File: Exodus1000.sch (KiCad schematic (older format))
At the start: 5 parts, among them J1 ARJ-169, M1 ET60S-02-24-02-X-VP-GP, M2 ET60S-02-24-02-X-VP-GP, M3 ET60S-02-24-02-X-VP-GP, M4 ET60S-02-24-02-X-VP-GP

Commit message: added some more stuff
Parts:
- removed J1: ARJ-169, Exodus_Connectors:ARJ-169, symbol Exodus_Connectors:ARJ-169
- removed M1, M2, M3, M4: ET60S-02-24-02-X-VP-GP, Exodus_Connectors:ET60S-02-24-02-X-VP-GP, symbol ET60S-02-24-02-X-VP-GP:ET60S-02-24-02-X-VP-GP
- added U4: TUSB4041I, Package_QFP:HTQFP-64-1EP_10x10mm_P0.5mm_EP8x8mm_Mask4.4x4.4mm_ThermalVias, symbol Interface_USB:TUSB4041I
- added U5: FSUSB42UMX, Package_DFN_QFN:MLPQ-16-1EP_4x4mm_P0.65mm_EP2.8x2.8mm, symbol FSUSB42UMX:FSUSB42UMX
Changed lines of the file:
@@
 $Descr A4 11693 8268
 encoding utf-8
-Sheet 1 3
+Sheet 1 4
 Title ""
 Date ""
@@
 Comment4 ""
 $EndDescr
-$Comp
-L ET60S-02-24-02-X-VP-GP:ET60S-02-24-02-X-VP-GP M2
-U 1 1 5C80BFD4
-P 9750 1100
-F 0 "M2" H 10278 -8  45  0000 L CNN
-F 1 "ET60S-02-24-02-X-VP-GP" H 10278 -92 45  0000 L CNN
-F 2 "Exodus_Connectors:ET60S-02-24-02-X-VP-GP" H 9780 1250 20  0001 C CNN
-F 3 "" H 9750 1100 50  0001 C CNN
-	1    9750 1100
-	1    0    0    -1
-$EndComp
-$Comp
-L ET60S-02-24-02-X-VP-GP:ET60S-02-24-02-X-VP-GP M2
-U 2 1 5C80C056
-P 8300 1350
-F 0 "M2" H 8750 1604 45  0000 C CNN
-F 1 "ET60S-02-24-02-X-VP-GP" H 8750 1520 45  0000 C CNN
-F 2 "Exodus_Connectors:ET60S-02-24-02-X-VP-GP" H 8330 1500 20  0001 C CNN
-F 3 "" H 8300 1350 50  0001 C CNN
-	2    8300 1350
-	1    0    0    -1
-$EndComp
-$Comp
-L ET60S-02-24-02-X-VP-GP:ET60S-02-24-02-X-VP-GP M1
-U 1 1 5C80C304
-P 1100 950
-F 0 "M1" H 1628 -158 45  0000 L CNN
-F 1 "ET60S-02-24-02-X-VP-GP" H 1628 -242 45  0000 L CNN
-F 2 "Exodus_Connectors:ET60S-02-24-02-X-VP-GP" H 1130 1100 20  0001 C CNN
-F 3 "" H 1100 950 50  0001 C CNN
-	1    1100 950
-	1    0    0    -1
-$EndComp
-$Comp
-L ET60S-02-24-02-X-VP-GP:ET60S-02-24-02-X-VP-GP M1
-U 2 1 5C80C3A6
-P 2050 1200
-F 0 "M1" H 2500 1454 45  0000 C CNN
-F 1 "ET60S-02-24-02-X-VP-GP" H 2500 1370 45  0000 C CNN
-F 2 "Exodus_Connectors:ET60S-02-24-02-X-VP-GP" H 2080 1350 20  0001 C CNN
-F 3 "" H 2050 1200 50  0001 C CNN
-	2    2050 1200
-	1    0    0    -1
-$EndComp
-$Comp
-L ET60S-02-24-02-X-VP-GP:ET60S-02-24-02-X-VP-GP M3
-U 1 1 5C80C5DA
-P 1100 3850
-F 0 "M3" H 1628 2742 45  0000 L CNN
-F 1 "ET60S-02-24-02-X-VP-GP" H 1628 2658 45  0000 L CNN
-F 2 "Exodus_Connectors:ET60S-02-24-02-X-VP-GP" H 1130 4000 20  0001 C CNN
-F 3 "" H 1100 3850 50  0001 C CNN
-	1    1100 3850
-	1    0    0    -1
-$EndComp
-$Comp
-L ET60S-02-24-02-X-VP-GP:ET60S-02-24-02-X-VP-GP M3
-U 2 1 5C80C63C
-P 2050 4050
-F 0 "M3" H 2500 4304 45  0000 C CNN
-F 1 "ET60S-02-24-02-X-VP-GP" H 2500 4220 45  0000 C CNN
-F 2 "Exodus_Connectors:ET60S-02-24-02-X-VP-GP" H 2080 4200 20  0001 C CNN
-F 3 "" H 2050 4050 50  0001 C CNN
-	2    2050 4050
-	1    0    0    -1
-$EndComp
-$Comp
-L ET60S-02-24-02-X-VP-GP:ET60S-02-24-02-X-VP-GP M4
-U 2 1 5C80C6A4
-P 8300 4150
-F 0 "M4" H 8750 4404 45  0000 C CNN
-F 1 "ET60S-02-24-02-X-VP-GP" H 8750 4320 45  0000 C CNN
-F 2 "Exodus_Connectors:ET60S-02-24-02-X-VP-GP" H 8330 4300 20  0001 C CNN
-F 3 "" H 8300 4150 50  0001 C CNN
-	2    8300 4150
-	1    0    0    -1
-$EndComp
-$Comp
-L ET60S-02-24-02-X-VP-GP:ET60S-02-24-02-X-VP-GP M4
-U 1 1 5C80C70C
-P 9800 3800
-F 0 "M4" H 10328 2692 45  0000 L CNN
-F 1 "ET60S-02-24-02-X-VP-GP" H 10328 2608 45  0000 L CNN
-F 2 "Exodus_Connectors:ET60S-02-24-02-X-VP-GP" H 9830 3950 20  0001 C CNN
-F 3 "" H 9800 3800 50  0001 C CNN
-	1    9800 3800
-	1    0    0    -1
-$EndComp
-$Comp
-L Exodus_Connectors:ARJ-169 J1
-U 1 1 5C80A95E
-P 7050 1750
-F 0 "J1" H 7050 2575 50  0000 C CNN
-F 1 "ARJ-169" H 7050 2484 50  0000 C CNN
-F 2 "Exodus_Connectors:ARJ-169" H 7200 1950 50  0001 C CNN
-F 3 "" H 7200 1950 50  0001 C CNN
-	1    7050 1750
-	1    0    0    -1
-$EndComp
-$Comp
-L Exodus_Connectors:ARJ-169 J1
-U 2 1 5C80A9FB
-P 7050 3150
-F 0 "J1" H 7050 3748 50  0000 C CNN
-F 1 "ARJ-169" H 7050 3657 50  0000 C CNN
-F 2 "Exodus_Connectors:ARJ-169" H 7200 3350 50  0001 C CNN
-F 3 "" H 7200 3350 50  0001 C CNN
-	2    7050 3150
-	1    0    0    -1
-$EndComp
 $Sheet
-S 3900 3250 850  850
+S 3300 2250 850  850
 U 5C80AE96
 F0 "TM4C129" 50
@@
 $EndSheet
 $Sheet
-S 5450 4250 900  800
+S 2750 3800 900  800
 U 5C80E9D1
 F0 "ft232h" 50
 F1 "ft232h.sch" 50
 $EndSheet
+$Sheet
+S 1250 2150 950  850
+U 5C8128A2
+F0 "Connectors" 50
+F1 "connectors.sch" 50
+$EndSheet
+$Comp
+L Interface_USB:TUSB4041I U4
+U 1 1 5C81313F
+P 6450 3450
+F 0 "U4" H 6450 1264 50  0000 C CNN
+F 1 "TUSB4041I" H 6450 1173 50  0000 C CNN
+F 2 "Package_QFP:HTQFP-64-1EP_10x10mm_P0.5mm_EP8x8mm_Mask4.4x4.4mm_ThermalVias" H 7650 5450 50  0001 L CNN
+F 3 "http://www.ti.com/lit/ds/symlink/tusb4041i.pdf" H 6150 3650 50  0001 C CNN
+	1    6450 3450
+	1    0    0    -1
+$EndComp
+$Comp
+L FSUSB42UMX:FSUSB42UMX U5
+U 1 1 5C81F656
+P 3050 6000
+F 0 "U5" H 3050 6767 50  0000 C CNN
+F 1 "FSUSB42UMX" H 3050 6676 50  0000 C CNN
+F 2 "Package_DFN_QFN:MLPQ-16-1EP_4x4mm_P0.65mm_EP2.8x2.8mm" H 3050 6000 50  0001 L BNN
+F 3 "ON Semiconductor" H 3050 6000 50  0001 L BNN
+F 4 "None" H 3050 6000 50  0001 L BNN "Field4"
+F 5 "Unavailable" H 3050 6000 50  0001 L BNN "Field5"
+F 6 "FSUSB42UMX" H 3050 6000 50  0001 L BNN "Field6"
+F 7 "UFQFN-10 ON Semiconductor" H 3050 6000 50  0001 L BNN "Field7"
+F 8 "FSUSB42 Series DPDT 4.3 V 480 Mbps SMT Hi Speed USB 2.0 Switch - UMLP-10" H 3050 6000 50  0001 L BNN "Field8"
+	1    3050 6000
+	1    0    0    -1
+$EndComp
 $EndSCHEMATC

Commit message: layout stuff
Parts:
- removed U4: TUSB4041I, Package_QFP:HTQFP-64-1EP_10x10mm_P0.5mm_EP8x8mm_Mask4.4x4.4mm_ThermalVias, symbol Interface_USB:TUSB4041I
- removed U5: FSUSB42UMX, Package_DFN_QFN:MLPQ-16-1EP_4x4mm_P0.65mm_EP2.8x2.8mm, symbol FSUSB42UMX:FSUSB42UMX
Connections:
- wire segments 0 -> 24
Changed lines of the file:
@@
 $EndDescr
 $Sheet
-S 3300 2250 850  850
+S 5450 2050 900  1450
 U 5C80AE96
 F0 "TM4C129" 50
 F1 "tm4c129.sch" 50
+F2 "ETH_RXI_N" I L 5450 2150 50
+F3 "ETH_RXI_P" I L 5450 2250 50
+F4 "ETH_TXO_N" I L 5450 2350 50
+F5 "ETH_TXO_P" I L 5450 2450 50
+F6 "JTAG_TCK" I R 6350 3100 50
+F7 "JTAG_TMS" I R 6350 3200 50
+F8 "JTAG_TDI" I R 6350 3300 50
+F9 "JTAG_TDO" I R 6350 3400 50
+F10 "USB_D_N" I L 5450 3050 50
+F11 "USB_D_P" I L 5450 3150 50
+F12 "USB_ID" I L 5450 3250 50
 $EndSheet
 $Sheet
-S 2750 3800 900  800
+S 5500 4250 900  800
 U 5C80E9D1
 F0 "ft232h" 50
 F1 "ft232h.sch" 50
+F2 "D-" I L 5500 4400 50
+F3 "D+" I L 5500 4500 50
 $EndSheet
 $Sheet
-S 1250 2150 950  850
+S 3850 2850 950  1350
 U 5C8128A2
 F0 "Connectors" 50
 F1 "connectors.sch" 50
+F2 "USB_OTG_N" I R 4800 3450 50
+F3 "USB_OTG_P" I R 4800 3550 50
+F4 "USB_JTAG_P" I R 4800 4000 50
+F5 "USB_JTAG_N" I R 4800 3900 50
+F6 "TD_P" I R 4800 3250 50
+F7 "TD_N" I R 4800 3150 50
+F8 "RD_P" I R 4800 3000 50
+F9 "RD_N" I R 4800 2900 50
 $EndSheet
-$Comp
-L Interface_USB:TUSB4041I U4
-U 1 1 5C81313F
-P 6450 3450
-F 0 "U4" H 6450 1264 50  0000 C CNN
-F 1 "TUSB4041I" H 6450 1173 50  0000 C CNN
-F 2 "Package_QFP:HTQFP-64-1EP_10x10mm_P0.5mm_EP8x8mm_Mask4.4x4.4mm_ThermalVias" H 7650 5450 50  0001 L CNN
-F 3 "http://www.ti.com/lit/ds/symlink/tusb4041i.pdf" H 6150 3650 50  0001 C CNN
-	1    6450 3450
-	1    0    0    -1
-$EndComp
-$Comp
-L FSUSB42UMX:FSUSB42UMX U5
-U 1 1 5C81F656
-P 3050 6000
-F 0 "U5" H 3050 6767 50  0000 C CNN
-F 1 "FSUSB42UMX" H 3050 6676 50  0000 C CNN
-F 2 "Package_DFN_QFN:MLPQ-16-1EP_4x4mm_P0.65mm_EP2.8x2.8mm" H 3050 6000 50  0001 L BNN
-F 3 "ON Semiconductor" H 3050 6000 50  0001 L BNN
-F 4 "None" H 3050 6000 50  0001 L BNN "Field4"
-F 5 "Unavailable" H 3050 6000 50  0001 L BNN "Field5"
-F 6 "FSUSB42UMX" H 3050 6000 50  0001 L BNN "Field6"
-F 7 "UFQFN-10 ON Semiconductor" H 3050 6000 50  0001 L BNN "Field7"
-F 8 "FSUSB42 Series DPDT 4.3 V 480 Mbps SMT Hi Speed USB 2.0 Switch - UMLP-10" H 3050 6000 50  0001 L BNN "Field8"
-	1    3050 6000
-	1    0    0    -1
-$EndComp
+Wire Wire Line
+	4800 4000 4950 4000
+Wire Wire Line
+	4950 4000 4950 4500
+Wire Wire Line
+	4950 4500 5500 4500
+Wire Wire Line
+	5500 4400 5100 4400
+Wire Wire Line
+	5100 4400 5100 3900
+Wire Wire Line
+	5100 3900 4800 3900
+Wire Wire Line
+	4800 3450 5150 3450
+Wire Wire Line
+	5150 3450 5150 3050
+Wire Wire Line
+	5150 3050 5450 3050
+Wire Wire Line
+	5450 3150 5250 3150
+Wire Wire Line
+	5250 3150 5250 3550
+Wire Wire Line
+	5250 3550 4800 3550
+Wire Wire Line
+	4800 2900 4850 2900
+Wire Wire Line
+	4850 2900 4850 2150
+Wire Wire Line
+	4850 2150 5450 2150
+Wire Wire Line
+	5450 2250 4900 2250
+Wire Wire Line
+	4900 2250 4900 3000
+Wire Wire Line
+	4900 3000 4800 3000
+Wire Wire Line
+	4800 3150 5000 3150
+Wire Wire Line
+	5000 3150 5000 2350
+Wire Wire Line
+	5000 2350 5450 2350
+Wire Wire Line
+	5450 2450 5050 2450
+Wire Wire Line
+	5050 2450 5050 3250
+Wire Wire Line
+	5050 3250 4800 3250
 $EndSCHEMATC

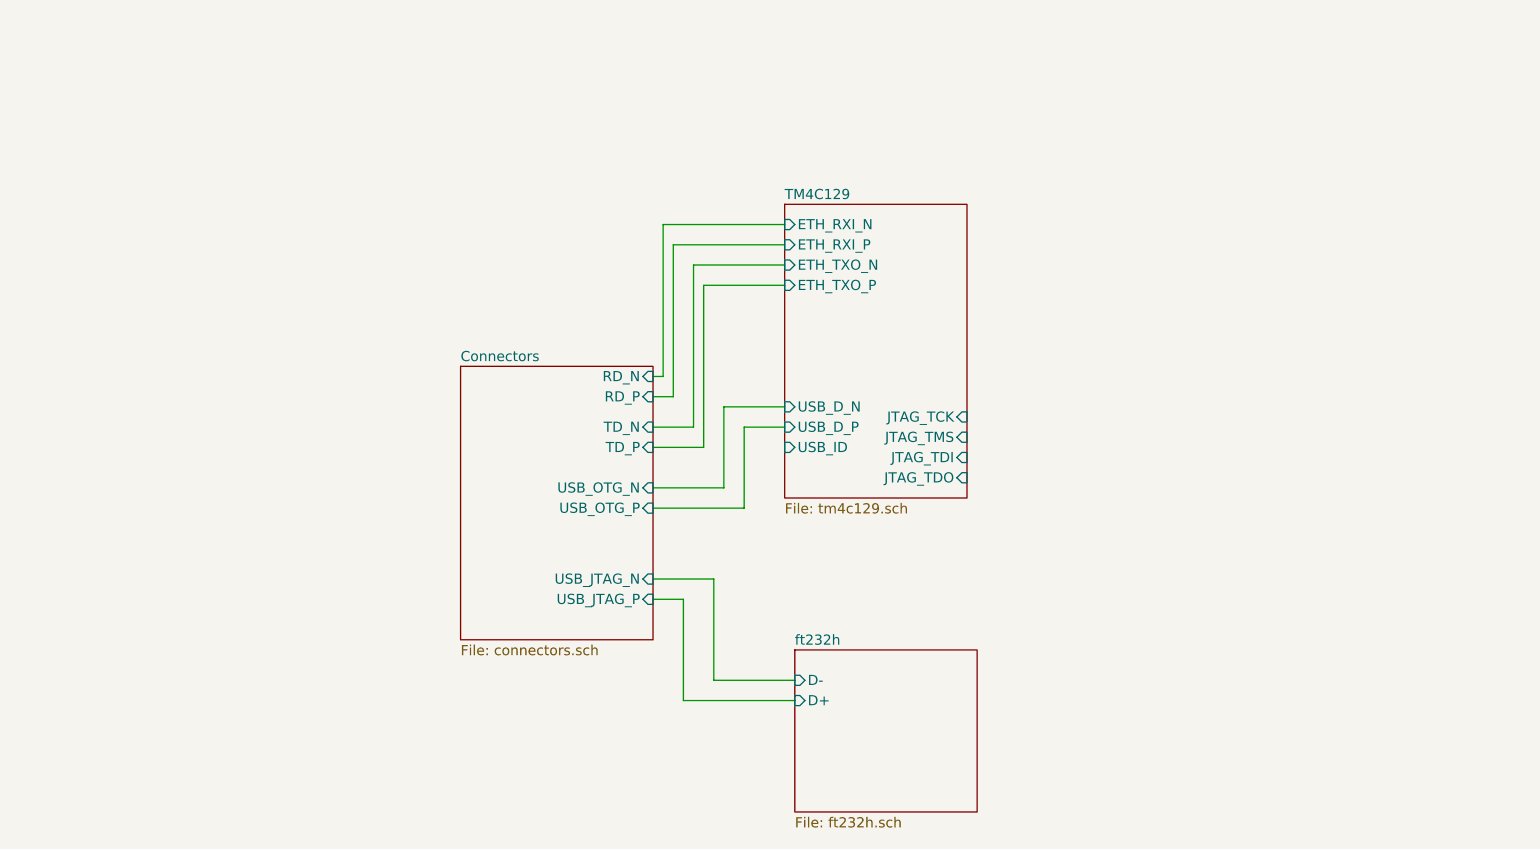
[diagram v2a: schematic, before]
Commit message: usb hub and sdram selected.
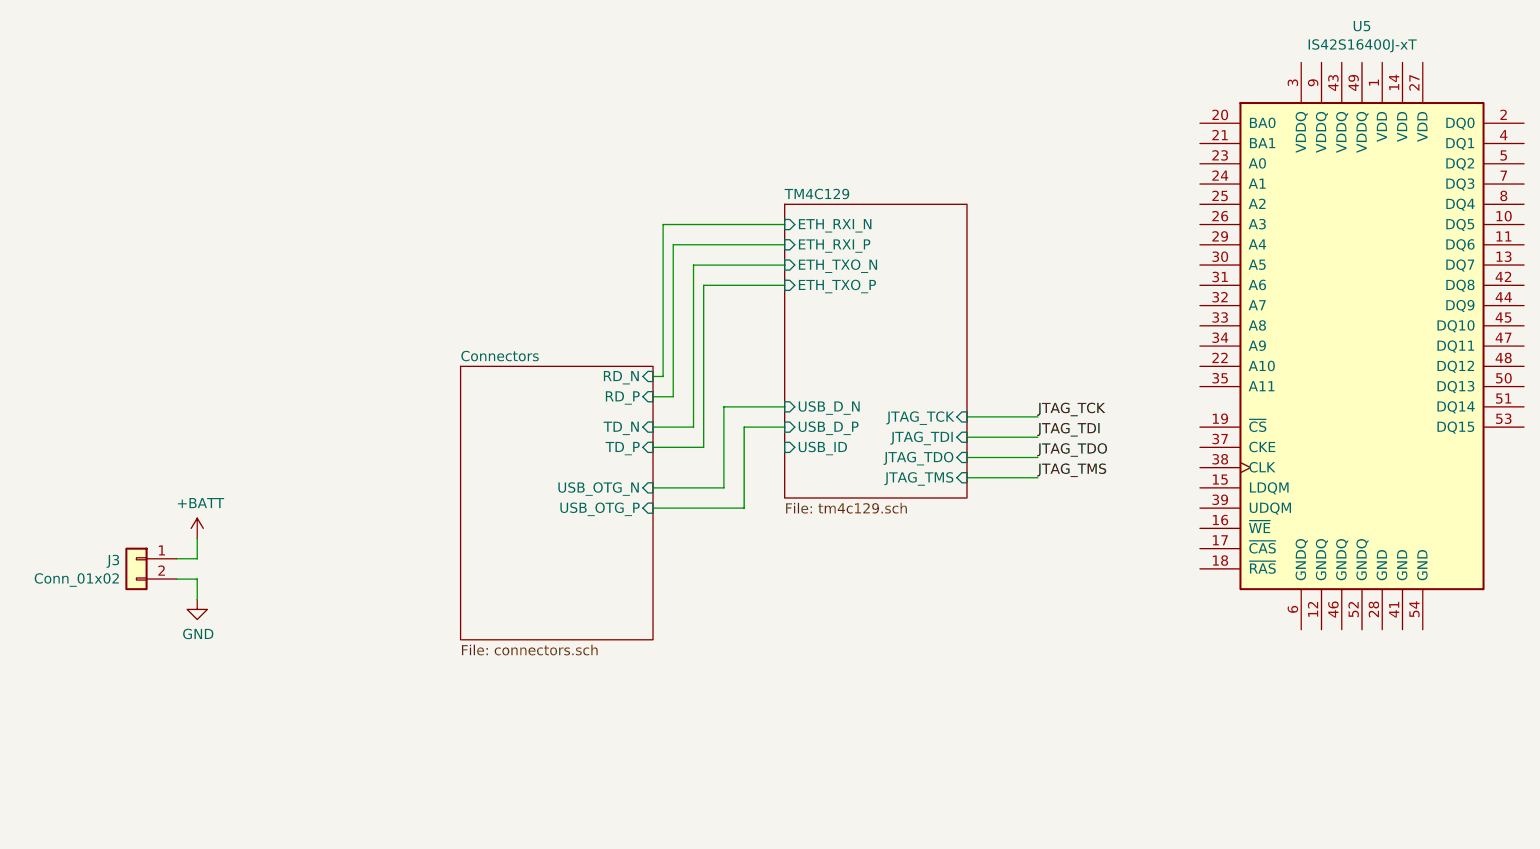
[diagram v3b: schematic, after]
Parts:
- added J3: Conn_01x02, Connector_PinHeader_2.54mm:PinHeader_1x02_P2.54mm_Horizontal, symbol Connector_Generic:Conn_01x02
- added U5: IS42S16400J-xT, Package_SO:TSOP-II-54_22.2x10.16mm_P0.8mm, symbol Memory_RAM:IS42S16400J-xT
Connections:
- new net +BATT: J3.1 (Pin_1)
- new net GND: J3.2 (Pin_2)
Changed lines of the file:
@@
 $Descr A4 11693 8268
 encoding utf-8
-Sheet 1 4
-Title ""
-Date ""
-Rev ""
-Comp ""
+Sheet 1 5
+Title "Exodus1000"
+Date "2019-03-16"
+Rev "A"
+Comp "Exodus"
 Comment1 ""
 Comment2 ""
@@
 F5 "ETH_TXO_P" I L 5450 2450 50
 F6 "JTAG_TCK" I R 6350 3100 50
-F7 "JTAG_TMS" I R 6350 3200 50
-F8 "JTAG_TDI" I R 6350 3300 50
-F9 "JTAG_TDO" I R 6350 3400 50
+F7 "JTAG_TMS" I R 6350 3400 50
+F8 "JTAG_TDI" I R 6350 3200 50
+F9 "JTAG_TDO" I R 6350 3300 50
 F10 "USB_D_N" I L 5450 3050 50
 F11 "USB_D_P" I L 5450 3150 50
 F12 "USB_ID" I L 5450 3250 50
-$EndSheet
-$Sheet
-S 5500 4250 900  800
-U 5C80E9D1
-F0 "ft232h" 50
-F1 "ft232h.sch" 50
-F2 "D-" I L 5500 4400 50
-F3 "D+" I L 5500 4500 50
 $EndSheet
 $Sheet
@@
 F2 "USB_OTG_N" I R 4800 3450 50
 F3 "USB_OTG_P" I R 4800 3550 50
-F4 "USB_JTAG_P" I R 4800 4000 50
-F5 "USB_JTAG_N" I R 4800 3900 50
-F6 "TD_P" I R 4800 3250 50
-F7 "TD_N" I R 4800 3150 50
-F8 "RD_P" I R 4800 3000 50
-F9 "RD_N" I R 4800 2900 50
+F4 "TD_P" I R 4800 3250 50
+F5 "TD_N" I R 4800 3150 50
+F6 "RD_P" I R 4800 3000 50
+F7 "RD_N" I R 4800 2900 50
 $EndSheet
-Wire Wire Line
-	4800 4000 4950 4000
-Wire Wire Line
-	4950 4000 4950 4500
-Wire Wire Line
-	4950 4500 5500 4500
-Wire Wire Line
-	5500 4400 5100 4400
-Wire Wire Line
-	5100 4400 5100 3900
-Wire Wire Line
-	5100 3900 4800 3900
 Wire Wire Line
 	4800 3450 5150 3450
@@
 Wire Wire Line
 	5050 3250 4800 3250
+Wire Wire Line
+	6350 3100 6700 3100
+Wire Wire Line
+	6350 3200 6700 3200
+Wire Wire Line
+	6350 3300 6700 3300
+Wire Wire Line
+	6350 3400 6700 3400
+Text Label 6700 3100 0    50   ~ 0
+JTAG_TCK
+Text Label 6700 3200 0    50   ~ 0
+JTAG_TDI
+Text Label 6700 3300 0    50   ~ 0
+JTAG_TDO
+Text Label 6700 3400 0    50   ~ 0
+JTAG_TMS
+$Comp
+L Connector_Generic:Conn_01x02 J3
+U 1 1 5C872DE6
+P 2250 3800
+F 0 "J3" H 2330 3792 50  0000 L CNN
+F 1 "Conn_01x02" H 2330 3701 50  0000 L CNN
+F 2 "Connector_PinHeader_2.54mm:PinHeader_1x02_P2.54mm_Horizontal" H 2250 3800 50  0001 C CNN
+F 3 "~" H 2250 3800 50  0001 C CNN
+	1    2250 3800
+	-1   0    0    -1
+$EndComp
+Wire Wire Line
+	2450 3800 2550 3800
+Wire Wire Line
+	2550 3800 2550 3700
+Wire Wire Line
+	2450 3900 2550 3900
+Wire Wire Line
+	2550 3900 2550 4000
+$Comp
+L power:GND #PWR0149
+U 1 1 5C8F5DB2
+P 2550 4000
+F 0 "#PWR0149" H 2550 3750 50  0001 C CNN
+F 1 "GND" H 2555 3827 50  0000 C CNN
+F 2 "" H 2550 4000 50  0001 C CNN
+F 3 "" H 2550 4000 50  0001 C CNN
+	1    2550 4000
+	1    0    0    -1
+$EndComp
+$Comp
+L power:+BATT #PWR0150
+U 1 1 5C8F5ED8
+P 2550 3700
+F 0 "#PWR0150" H 2550 3550 50  0001 C CNN
+F 1 "+BATT" H 2565 3873 50  0000 C CNN
+F 2 "" H 2550 3700 50  0001 C CNN
+F 3 "" H 2550 3700 50  0001 C CNN
+	1    2550 3700
+	1    0    0    -1
+$EndComp
+$Comp
+L Memory_RAM:IS42S16400J-xT U5
+U 1 1 5CA3FBF0
+P 8300 2750
+F 0 "U5" H 8300 4328 50  0000 C CNN
+F 1 "IS42S16400J-xT" H 8300 4237 50  0000 C CNN
+F 2 "Package_SO:TSOP-II-54_22.2x10.16mm_P0.8mm" H 8300 2750 50  0001 C CNN
+F 3 "http://www.issi.com/WW/pdf/42-45S16400J.pdf" H 7700 4000 50  0001 C CNN
+	1    8300 2750
+	1    0    0    -1
+$EndComp
 $EndSCHEMATC
